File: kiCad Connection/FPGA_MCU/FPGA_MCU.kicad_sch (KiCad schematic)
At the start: 3 parts, among them U1 CN7, U2 CN10, U3 CMOD_A7

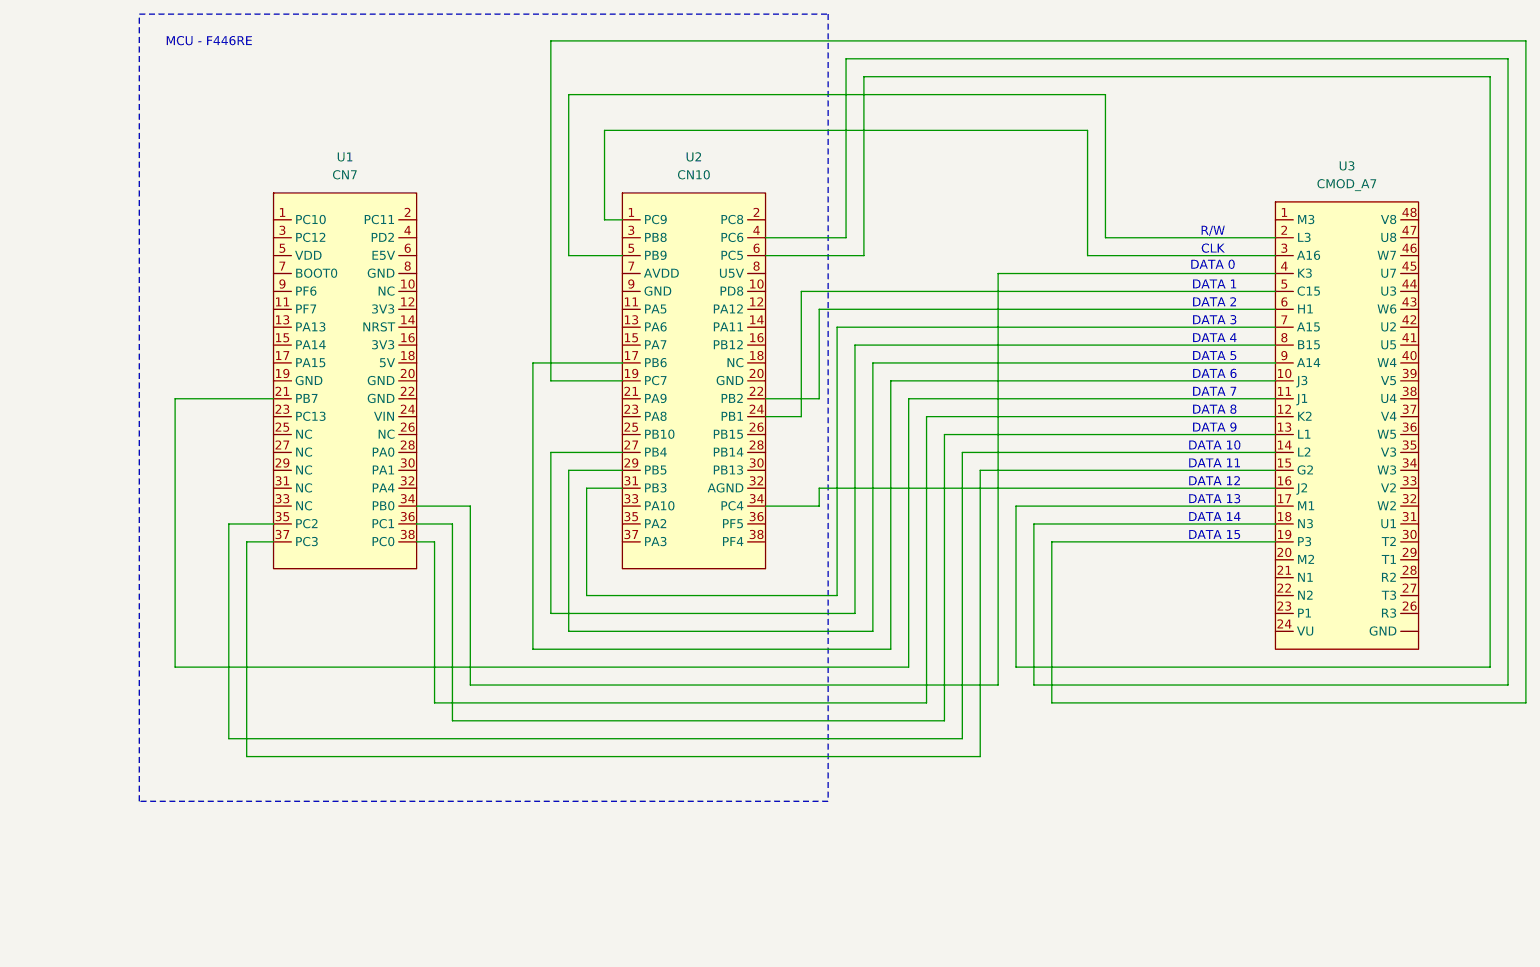
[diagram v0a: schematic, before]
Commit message: added the DAC vivado project
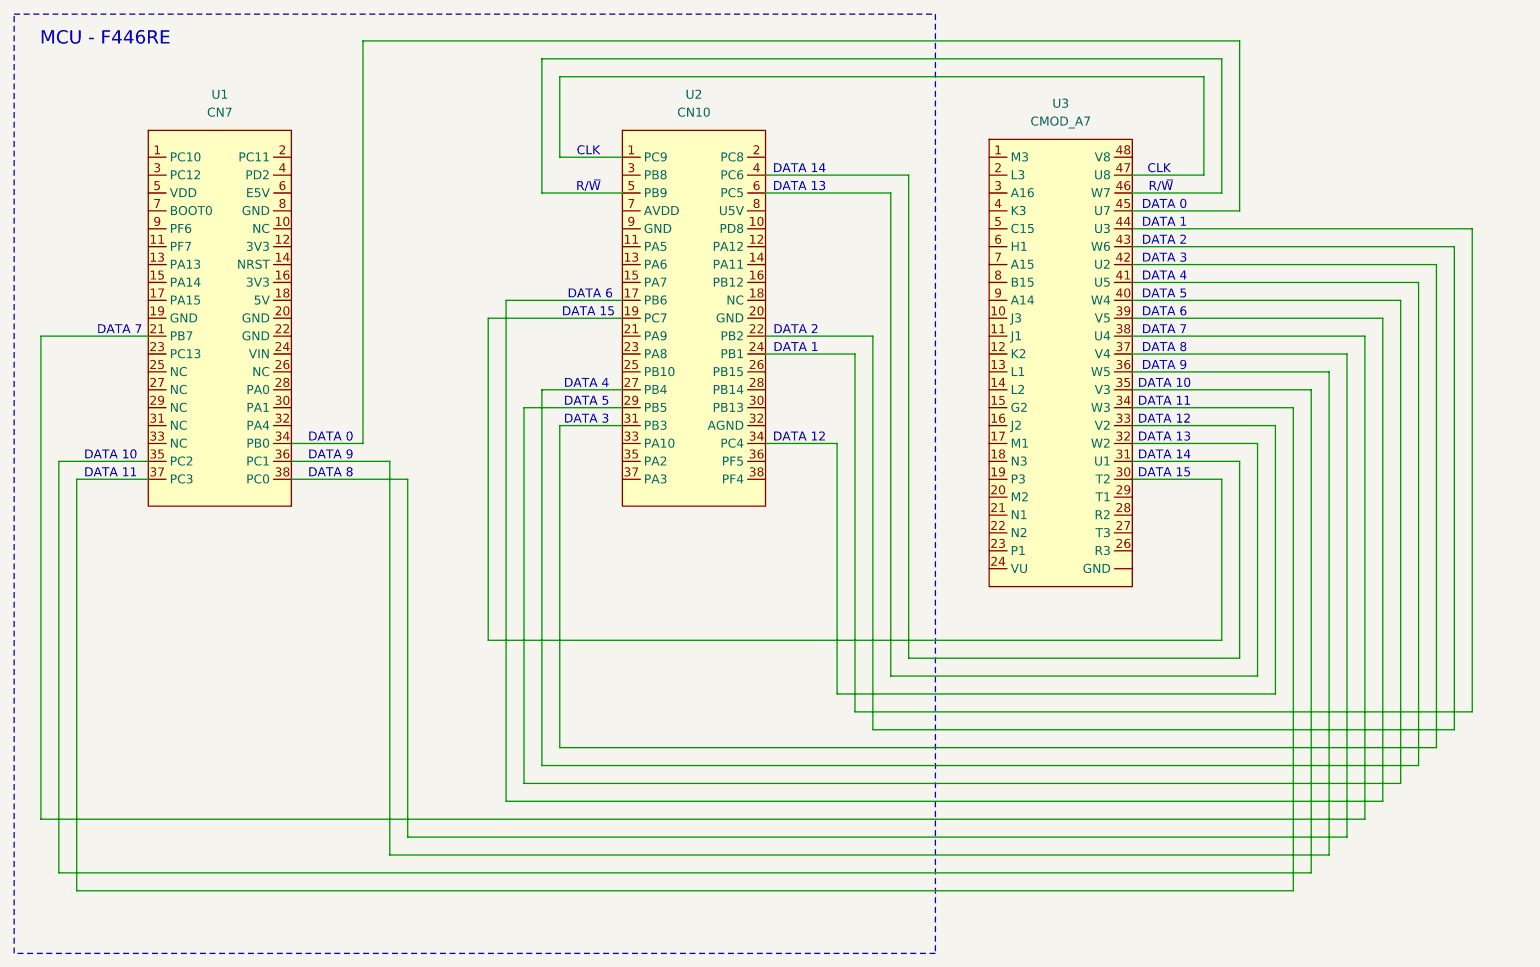
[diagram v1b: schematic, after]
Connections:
- net at U3.10 (J3): no longer U2.17 (PB6)
- net at U3.11 (J1): no longer U1.21 (PB7)
- net at U3.12 (K2): no longer U1.38 (PC0)
- net at U3.13 (L1): no longer U1.36 (PC1)
- net at U3.14 (L2): no longer U1.35 (PC2)
- net at U3.15 (G2): no longer U1.37 (PC3)
- net at U3.16 (J2): no longer U2.34 (PC4)
- net at U3.17 (M1): no longer U2.6 (PC5)
- net at U3.18 (N3): no longer U2.4 (PC6)
- net at U3.19 (P3): no longer U2.19 (PC7)
- net at U3.2 (L3): no longer U2.5 (PB9)
- net at U3.3 (A16): no longer U2.1 (PC9)
- net at U3.30 (T2): now also U2.19 (PC7)
- net at U3.31 (U1): now also U2.4 (PC6)
- net at U3.32 (W2): now also U2.6 (PC5)
- net at U3.33 (V2): now also U2.34 (PC4)
- net at U3.34 (W3): now also U1.37 (PC3)
- net at U3.35 (V3): now also U1.35 (PC2)
- net at U3.36 (W5): now also U1.36 (PC1)
- net at U3.37 (V4): now also U1.38 (PC0)
- net at U3.38 (U4): now also U1.21 (PB7)
- net at U3.39 (V5): now also U2.17 (PB6)
- net at U3.4 (K3): no longer U1.34 (PB0)
- net at U3.40 (W4): now also U2.29 (PB5)
- net at U3.41 (U5): now also U2.27 (PB4)
- net at U3.42 (U2): now also U2.31 (PB3)
- net at U3.43 (W6): now also U2.22 (PB2)
- net at U3.44 (U3): now also U2.24 (PB1)
- net at U3.45 (U7): now also U1.34 (PB0)
- net at U3.46 (W7): now also U2.5 (PB9)
- net at U3.47 (U8): now also U2.1 (PC9)
- net at U3.5 (C15): no longer U2.24 (PB1)
- net at U3.6 (H1): no longer U2.22 (PB2)
- net at U3.7 (A15): no longer U2.31 (PB3)
- net at U3.8 (B15): no longer U2.27 (PB4)
- net at U3.9 (A14): no longer U2.29 (PB5)
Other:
- note added: "_"
- moved on the sheet: U1, U2, U3

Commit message: minor changes
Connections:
- net at U3.48 (V8): now also U2.2 (PC8)
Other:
- note added: "IX"
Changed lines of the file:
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@@
+	(wire
+		(pts
+			(xy 173.99 49.53) (xy 181.61 49.53)
+		)
+		(stroke
+			(width 0)
+			(type default)
+		)
+	)
 	(wire
 		(pts
@@
 	(wire
 		(pts
+			(xy 181.61 40.64) (xy 142.24 40.64)
+		)
+		(stroke
+			(width 0)
+			(type default)
+		)
+	)
+	(wire
+		(pts
+			(xy 142.24 40.64) (xy 142.24 49.53)
+		)
+		(stroke
+			(width 0)
+			(type default)
+		)
+	)
+	(wire
+		(pts
 			(xy 132.08 125.73) (xy 194.31 125.73)
 		)
@@
 	(wire
 		(pts
+			(xy 142.24 49.53) (xy 121.92 49.53)
+		)
+		(stroke
+			(width 0)
+			(type default)
+		)
+	)
+	(wire
+		(pts
 			(xy 90.17 54.61) (xy 90.17 35.56)
 		)
@@
 		(pts
 			(xy 121.92 74.93) (xy 137.16 74.93)
+		)
+		(stroke
+			(width 0)
+			(type default)
+		)
+	)
+	(wire
+		(pts
+			(xy 181.61 49.53) (xy 181.61 40.64)
 		)
 		(stroke
@@
 		(effects
 			(font
+				(size 1.27 1.27)
+			)
+		)
+	)
+	(text "IX"
+		(exclude_from_sim no)
+		(at 123.952 48.514 0)
+		(effects
+			(font
